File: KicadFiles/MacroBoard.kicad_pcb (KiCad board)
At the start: 2 copper layers, 94 x 115.6 mm, 79 parts, among them J1 USB_B_Micro, J2 Conn_01x08_Male, SW1 SW_Push, SW10 SW_Push, SW11 SW_Push, SW12 SW_Push, SW13 SW_Push, SW14 SW_Push, SW15 SW_Push, SW16 SW_Push, SW17 RotaryEncoder_Switch, SW2 SW_Push, SW3 SW_Push, SW4 SW_Push, SW5 SW_Push, SW6 SW_Push, SW7 SW_Push, SW8 SW_Push, SW9 SW_Push, U1 STM32F103C6Tx, U2 TC1262-33, Y1 8MHz

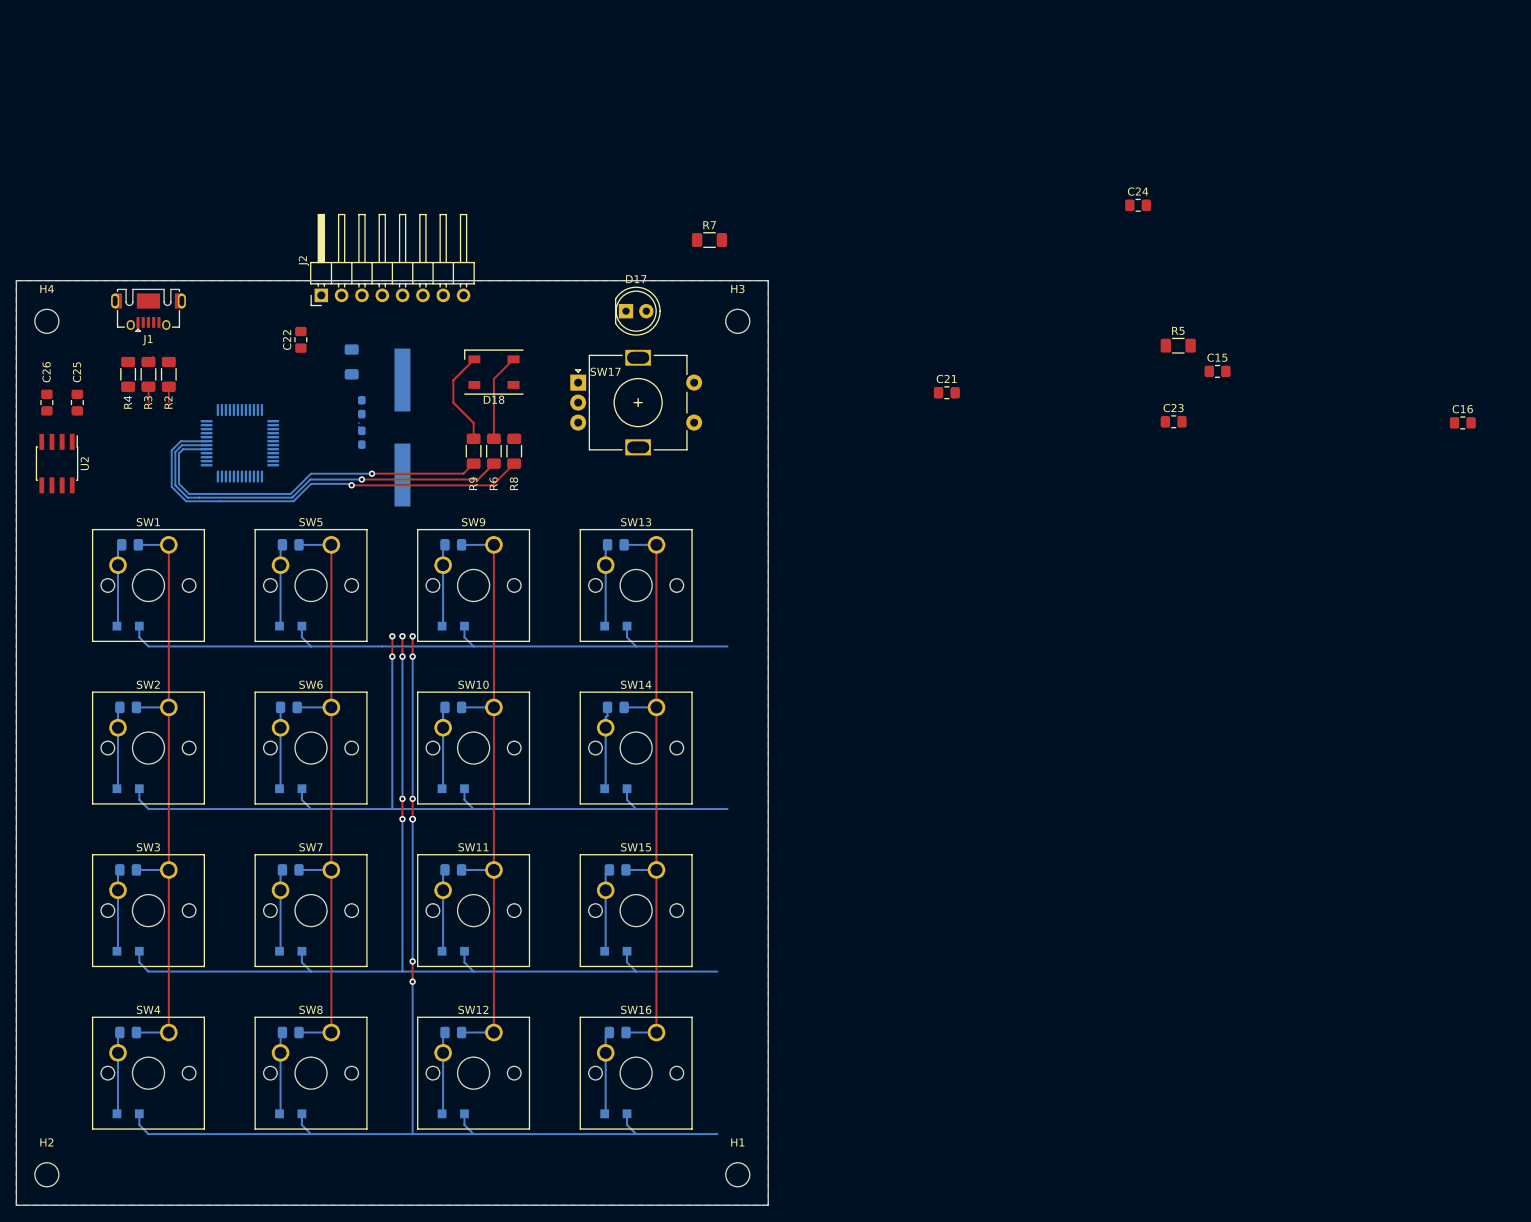
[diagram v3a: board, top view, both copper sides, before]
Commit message: placed all components
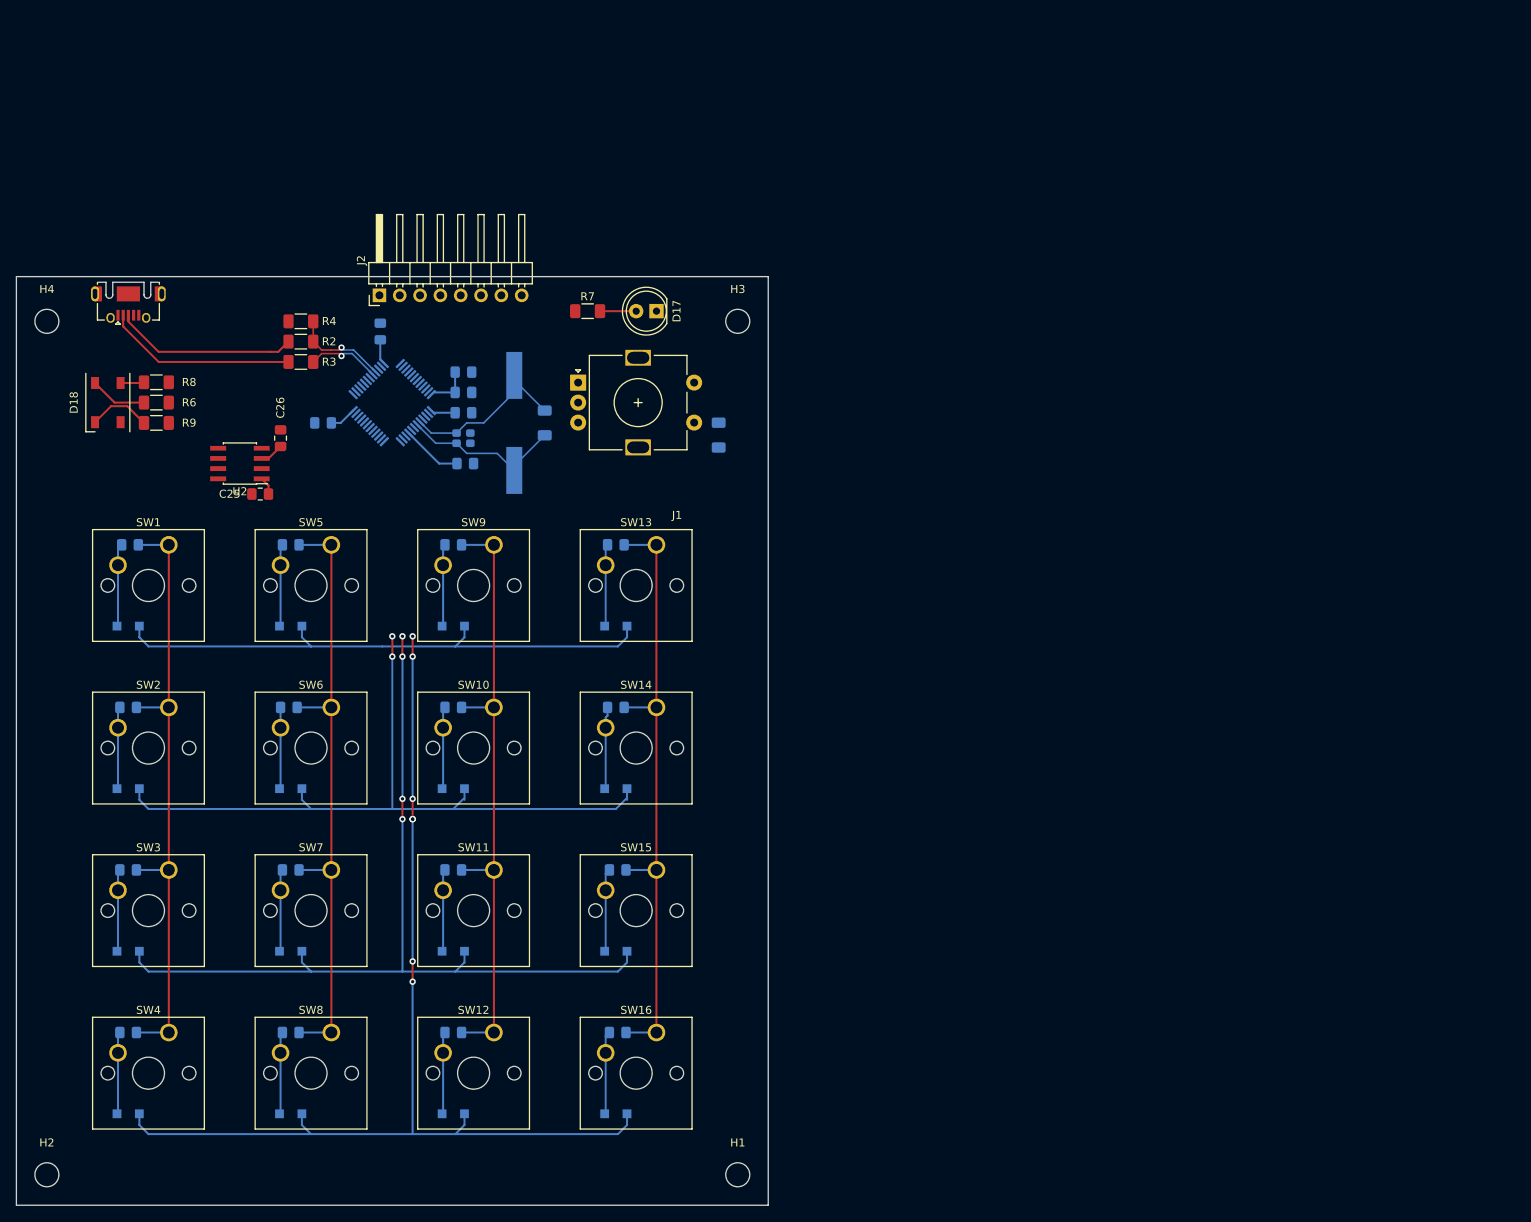
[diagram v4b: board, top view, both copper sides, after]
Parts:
- C15, C16, C21, C22, C23, C24, R5: moved to B.Cu
- moved C16 124.8 mm to (72.6, 68.6)
- moved C15 94.4 mm to (72.4, 62.2)
- moved C23 88.9 mm to (72.4, 59.7)
- moved C24 86.9 mm to (72.4, 57.1)
- moved C21 78.1 mm to (54.8, 63.5), turned to 180 degrees
- moved R5 58.5 mm to (104.3, 65.0), turned to 90 degrees
- moved D18 48.4 mm to (27.9, 61.0), turned to -90 degrees
- moved R8 45.6 mm to (34.0, 58.4), turned to 180 degrees
- moved R6 42.6 mm to (34.0, 61.0), turned to 180 degrees
- moved R9 39.8 mm to (34.0, 63.5), turned to 180 degrees
- moved C26 29.5 mm to (49.5, 65.4)
- moved C25 25.6 mm to (47.0, 72.4), turned to 180 degrees
- moved R1 25.3 mm to (82.5, 63.5), turned to -90 degrees
- moved U2 22.9 mm to (44.5, 68.6), turned to 180 degrees
- moved R4 22.6 mm to (52.1, 50.8), turned to 0 degrees
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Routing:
- net led_green: track 55.1 -> 0.00 mm, vias 1 -> 0
- net led_blue: track 50.7 -> 0.00 mm, vias 1 -> 0
- net led_red: track 46.4 -> 0.00 mm, vias 1 -> 0
- net VBAT: track 0.00 -> 25.8 mm
- net Net-(J1-Pad3): track 0.00 -> 23.2 mm
- net Net-(J1-Pad2): track 0.88 -> 23.9 mm
- net Crystal+: track 0.00 -> 22.5 mm
- net Crystal-: track 0.00 -> 20.5 mm
- net ROW0: track 84.4 -> 70.7 mm
- net ROW1: track 106.0 -> 92.4 mm
- net ROW3: track 145.4 -> 133.0 mm
- net ROW2: track 125.1 -> 112.6 mm
- net USBD+: track 2.02 -> 12.2 mm, vias 0 -> 1
- net USBD-: track 1.98 -> 9.27 mm, vias 0 -> 1
- net Net-(D17-Pad2): track 0.00 -> 4.52 mm
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- removed copper zone on B.Cu, net GND
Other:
- board size 94 x 115.6 mm -> 94 x 116.1 mm

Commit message: before flipping columns
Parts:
- R5: moved to F.Cu
- moved C25 9.96 mm to (37.6, 69.1), turned to 90 degrees
- moved J2 7.34 mm to (54.6, 46.5)
- moved C26 5.30 mm to (45.7, 69.1)
- moved R2 5.08 mm to (47.0, 53.3)
- moved R3 5.08 mm to (47.0, 55.9)
- moved R4 5.08 mm to (47.0, 50.8)
- moved U2 3.18 mm to (41.7, 67.1), turned to 90 degrees
- moved C22 0.87 mm to (62.0, 52.9)
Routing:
- net VBAT: track 25.8 -> 115.1 mm, vias 0 -> 3
- net ROW3: track 133.0 -> 70.7 mm, vias 7 -> 0
- net +5V: track 2.26 -> 44.4 mm, vias 0 -> 2
- net ROW2: track 112.6 -> 70.7 mm, vias 4 -> 0
- net led_red: track 0.00 -> 27.1 mm, vias 0 -> 1
- net RotaryA: track 0.00 -> 26.8 mm, vias 0 -> 1
- net led_green: track 0.00 -> 26.7 mm, vias 0 -> 1
- net led_blue: track 0.00 -> 26.7 mm, vias 0 -> 1
- net RotaryB: track 0.00 -> 26.0 mm, vias 0 -> 1
- net ROW1: track 92.4 -> 71.4 mm, vias 2 -> 0
- net SWDIO: track 0.00 -> 12.3 mm
- net COL3: track 76.7 -> 84.9 mm
- net COL2: track 77.1 -> 84.8 mm
- net COL1: track 77.4 -> 84.4 mm
- net DebugLED: track 0.00 -> 6.85 mm, vias 0 -> 1
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- added copper zone on B.Cu, net GND
- added copper zone on F.Cu, net GND

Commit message: flipped columns, connected columns and rows and programming pins in pcb
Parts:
- moved R7 9.73 mm to (97.6, 49.9), turned to 180 degrees
- moved D17 7.50 mm to (89.0, 49.9), turned to 0 degrees
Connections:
- U1 pad 13: COL0 -> COL3
- U1 pad 14: COL1 -> COL2
- U1 pad 15: COL2 -> COL1
- U1 pad 16: COL3 -> COL0
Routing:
- net ROW3: track 70.7 -> 170.0 mm, vias 0 -> 2
- net ROW2: track 70.7 -> 148.6 mm, vias 0 -> 2
- net DebugLED: track 6.85 -> 78.6 mm
- net ROW1: track 71.4 -> 127.4 mm, vias 0 -> 2
- net GND: track 0.00 -> 38.1 mm, vias 0 -> 4
- net COL3: track 84.9 -> 121.4 mm
- net ROW0: track 70.8 -> 106.0 mm, vias 0 -> 2
- net COL0: track 83.6 -> 113.1 mm
- net JTDI: track 0.00 -> 21.8 mm, vias 0 -> 2
- net NRST: track 0.00 -> 19.7 mm, vias 0 -> 1
- net JTDO: track 0.00 -> 18.9 mm, vias 0 -> 1
- net COL2: track 84.8 -> 102.5 mm
- net +5V: track 44.4 -> 60.6 mm
- net BOOT0: track 0.00 -> 13.2 mm
- net VBAT: track 115.1 -> 126.1 mm
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
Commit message: i hope it's finished
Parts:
- moved H3 1.78 mm to (106.7, 49.0)
- moved H4 1.78 mm to (20.3, 49.0)
- moved C21 1.25 mm to (53.6, 63.5)
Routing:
- net VBAT: track 126.1 -> 137.6 mm, vias 3 -> 5
- net GND: track 38.1 -> 47.8 mm, vias 4 -> 5

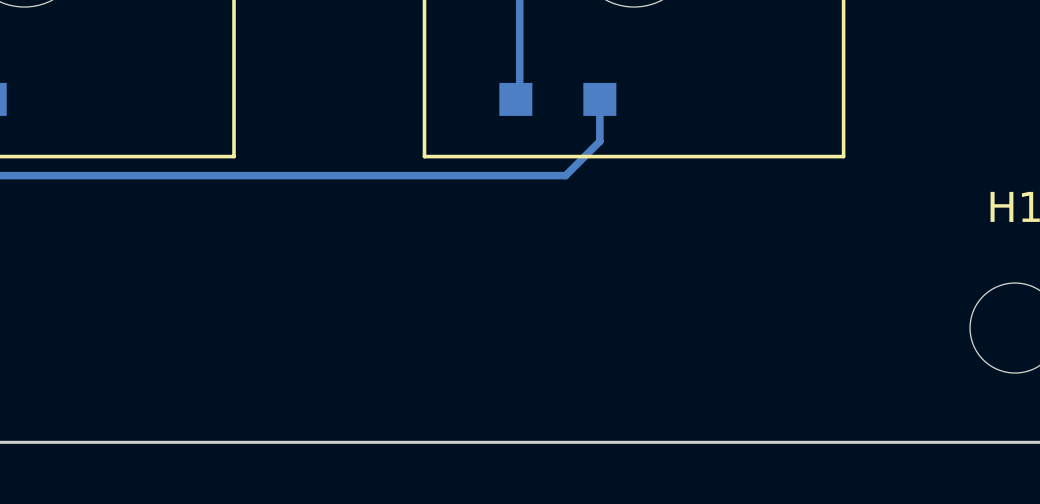
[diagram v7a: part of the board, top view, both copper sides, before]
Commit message: signing on silkscreen
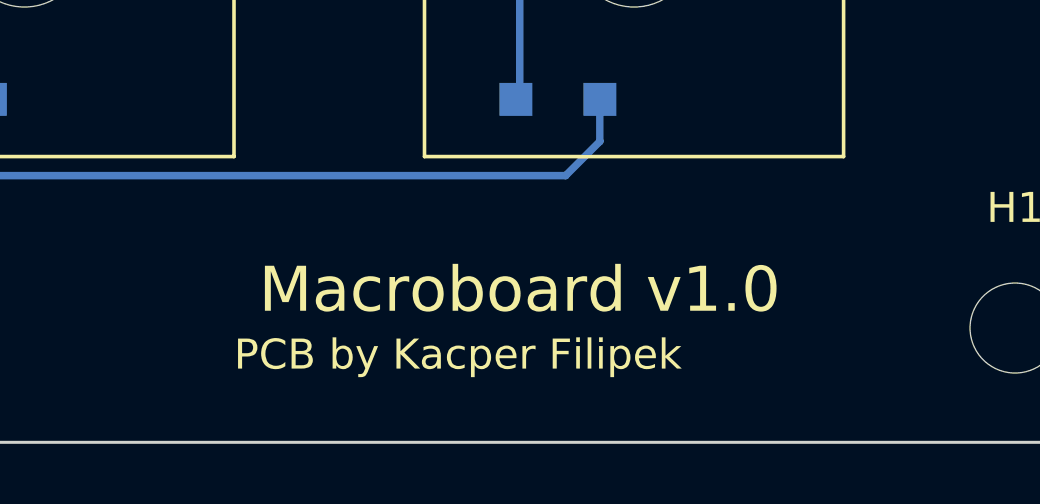
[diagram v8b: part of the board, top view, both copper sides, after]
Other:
- board text added: "Macroboard v1.0"
- board text added: "PCB by Kacper Filipek"
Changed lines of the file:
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@@
   )
   (gr_rect (start 16.51 45.212) (end 110.49 161.29) (layer "Edge.Cuts") (width 0.1) (fill none))
+  (gr_text "Macroboard v1.0" (at 90.17 156.21) (layer "F.SilkS")
+    (effects (font (size 1.5 1.5) (thickness 0.3)))
+  )
+  (gr_text "PCB by Kacper Filipek\n" (at 80.645 158.369) (layer "F.SilkS")
+    (effects (font (size 1 1) (thickness 0.2)) (justify left))
+  )
   (segment (start 31.81 50.045) (end 31.81 48.67) (width 0.25) (layer "F.Cu") (net 1))
   (segment (start 31.81 48.67) (end 30.51 47.37) (width 0.25) (layer "F.Cu") (net 1))
